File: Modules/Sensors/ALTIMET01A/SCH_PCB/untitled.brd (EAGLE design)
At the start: 20.1 x 40.4 mm, 11 parts, among them X1 FFF

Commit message: 
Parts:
- C1, C3: value (none) -> 100nF
- C2: value (none) -> 10uF
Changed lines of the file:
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@@
 <attribute name="NAME" x="8.66" y="14.79" size="1.27" layer="26" rot="MR180"/>
 </element>
-<element name="C1" library="rcl" package="C0805" value="" x="3.59" y="15.75" smashed="yes" rot="MR270">
+<element name="C1" library="rcl" package="C0805" value="100nF" x="3.59" y="15.75" smashed="yes" rot="MR270">
 <attribute name="VALUE" x="6.13" y="17.02" size="1.27" layer="28" rot="MR270"/>
 </element>
-<element name="C2" library="rcl" package="C0805" value="" x="6" y="15.75" smashed="yes" rot="MR270">
+<element name="C2" library="rcl" package="C0805" value="10uF" x="6" y="15.75" smashed="yes" rot="MR270">
 <attribute name="NAME" x="7.42" y="13.12" size="1.27" layer="26" rot="MR0"/>
 <attribute name="VALUE" x="8.54" y="17.02" size="1.27" layer="28" rot="MR270"/>
 </element>
-<element name="C3" library="rcl" package="C0805" value="" x="4.74" y="12.12" smashed="yes" rot="MR0">
+<element name="C3" library="rcl" package="C0805" value="100nF" x="4.74" y="12.12" smashed="yes" rot="MR0">
 <attribute name="NAME" x="6.01" y="9.64" size="1.27" layer="26" rot="MR0"/>
 <attribute name="VALUE" x="6.01" y="9.58" size="1.27" layer="28" rot="MR0"/>

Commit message: 
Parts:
- X1: value FFF -> MPL3115A2
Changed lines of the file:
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@@
 </autorouter>
 <elements>
-<element name="X1" library="moje_cidla" package="LGA" value="FFF" x="9.84" y="14.26" smashed="yes" rot="MR180">
+<element name="X1" library="moje_cidla" package="LGA" value="MPL3115A2" x="9.84" y="14.26" smashed="yes" rot="MR180">
 <attribute name="NAME" x="8.66" y="14.79" size="1.27" layer="26" rot="MR180"/>
 </element>

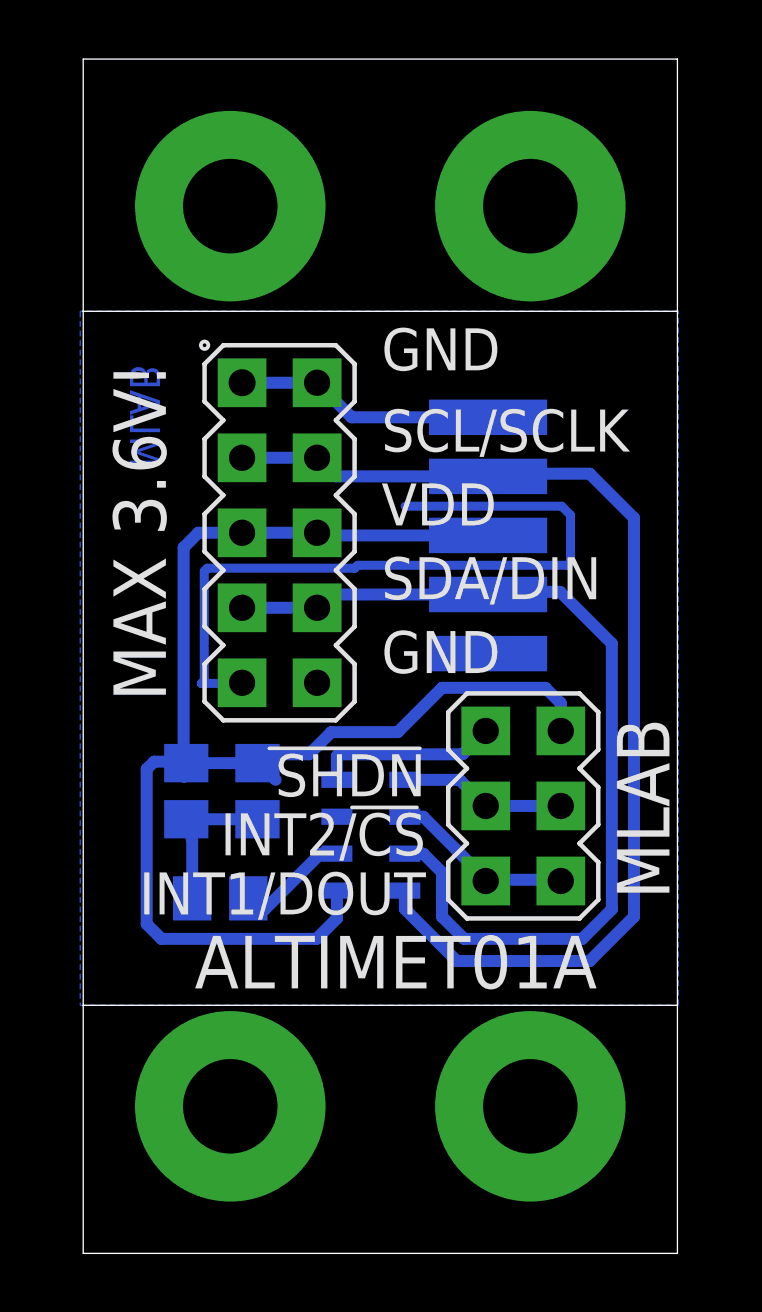
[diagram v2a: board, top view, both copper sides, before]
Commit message: 
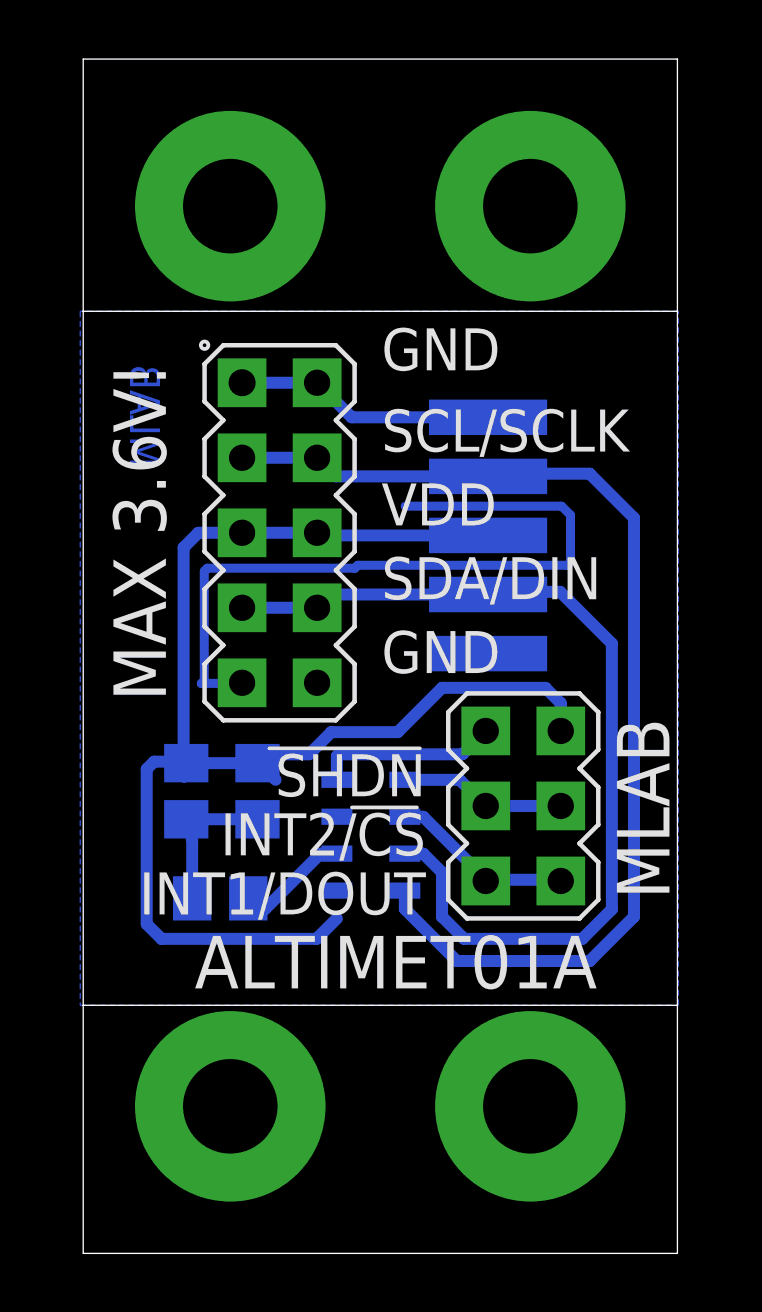
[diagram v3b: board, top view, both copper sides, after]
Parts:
- X2, X3, X4, X5: value (none) -> SROUB3M
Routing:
- net VCC: track 49.6 -> 48.5 mm
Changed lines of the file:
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@@
 </element>
 <element name="SV3" library="moje_hrebinky" package="SMD_MA05-1" value="" x="13.81" y="24.41" smashed="yes" rot="MR0"/>
-<element name="X2" library="moje" package="SROUB3M" value="" x="5.08" y="5.08"/>
-<element name="X3" library="moje" package="SROUB3M" value="" x="15.24" y="5.08"/>
-<element name="X4" library="moje" package="SROUB3M" value="" x="5.08" y="35.56" rot="R180"/>
-<element name="X5" library="moje" package="SROUB3M" value="" x="15.24" y="35.56"/>
+<element name="X2" library="moje" package="SROUB3M" value="SROUB3M" x="5.08" y="5.08"/>
+<element name="X3" library="moje" package="SROUB3M" value="SROUB3M" x="15.24" y="5.08"/>
+<element name="X4" library="moje" package="SROUB3M" value="SROUB3M" x="5.08" y="35.56" rot="R180"/>
+<element name="X5" library="moje" package="SROUB3M" value="SROUB3M" x="15.24" y="35.56"/>
 <element name="SV1" library="moje_hrebinky" package="MA05-2" value="" x="6.75" y="24.5" smashed="yes" rot="R270">
 <attribute name="OC_NEWARK" value="unknown" x="6.75" y="24.5" size="1.778" layer="27" rot="R270" display="off"/>
@@
 <contactref element="C1" pad="1"/>
 <contactref element="C2" pad="1"/>
-<contactref element="X1" pad="VDD"/>
 <wire x1="3.54" y1="16.25" x2="3.59" y2="16.7" width="0.4064" layer="16"/>
 <contactref element="SV1" pad="6"/>
@@
 <wire x1="3.54" y1="16.25" x2="3.5" y2="16.25" width="0.4064" layer="16"/>
 <wire x1="3.5" y1="16.25" x2="3.25" y2="16.5" width="0.4064" layer="16"/>
-<wire x1="8.69" y1="12.385" x2="8.69" y2="12.19" width="0.4064" layer="16"/>
 <wire x1="2.75" y1="10.75" x2="2.25" y2="11.25" width="0.4064" layer="16"/>
 <wire x1="2.25" y1="11.25" x2="2.25" y2="16.5" width="0.4064" layer="16"/>
@@
 <wire x1="7.75" y1="17" x2="6.3" y2="17" width="0.4064" layer="16"/>
 <wire x1="6.3" y1="17" x2="6" y2="16.7" width="0.4064" layer="16"/>
-<wire x1="8.69" y1="12.385" x2="8.69" y2="11.44" width="0.4064" layer="16"/>
 <wire x1="8.69" y1="11.44" x2="8" y2="10.75" width="0.4064" layer="16"/>
 <wire x1="8" y1="10.75" x2="2.75" y2="10.75" width="0.4064" layer="16"/>
+<contactref element="X1" pad="VDD"/>
+<wire x1="8.69" y1="11.44" x2="8.69" y2="12.385" width="0" layer="19" extent="16-16"/>
 </signal>
 <signal name="N$3">
